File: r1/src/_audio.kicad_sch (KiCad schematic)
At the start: 24 parts, among them J10 PJ-320D, U7 PAM8908, U8 PCM5100A

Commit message: Assign MPN's and LCSC part numbers
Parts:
- D? (x2): LCSC (none) -> C261278
- J10: LCSC (none) -> C431535; MPN (none) -> PJ-320D
- U7: LCSC (none) -> C33233; MPN (none) -> PAM8908
- U8: value PCM5100A -> PCM5100APW; LCSC (none) -> C1540069; MPN (none) -> PCM5100APWR
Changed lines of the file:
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@@
       (effects (font (size 1.27 1.27)))
     )
-    (property "Value" "PCM5100A" (at 102.87 77.47 0)
+    (property "Value" "PCM5100APW" (at 102.87 77.47 0)
       (effects (font (size 1.27 1.27)))
     )
@@
     )
     (property "Datasheet" "http://www.ti.com/lit/ds/symlink/pcm5100.pdf" (at 92.71 73.66 0)
+      (effects (font (size 1.27 1.27)) hide)
+    )
+    (property "MPN" "PCM5100APWR" (at 93.98 92.71 0)
+      (effects (font (size 1.27 1.27)) hide)
+    )
+    (property "LCSC" "C1540069" (at 93.98 92.71 0)
       (effects (font (size 1.27 1.27)) hide)
     )
@@
       (effects (font (size 1.27 1.27)) hide)
     )
+    (property "MPN" "PAM8908" (at 180.34 99.06 0)
+      (effects (font (size 1.27 1.27)) hide)
+    )
+    (property "LCSC" "C33233" (at 180.34 99.06 0)
+      (effects (font (size 1.27 1.27)) hide)
+    )
     (pin "1")
     (pin "10")
@@
       (effects (font (size 1.27 1.27)) hide)
     )
+    (property "LCSC" "C261278" (at 222.25 93.98 0)
+      (effects (font (size 1.27 1.27)) hide)
+    )
     (pin "1")
     (pin "2")
@@
       (effects (font (size 1.27 1.27)) hide)
     )
+    (property "LCSC" "C261278" (at 214.63 93.98 0)
+      (effects (font (size 1.27 1.27)) hide)
+    )
     (pin "1")
     (pin "2")
@@
       (effects (font (size 1.27 1.27)) hide)
     )
+    (property "MPN" "PJ-320D" (at 236.22 90.17 0)
+      (effects (font (size 1.27 1.27)) hide)
+    )
+    (property "LCSC" "C431535" (at 236.22 90.17 0)
+      (effects (font (size 1.27 1.27)) hide)
+    )

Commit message: Assign manufacturers
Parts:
- J10: Manufacturer (none) -> HRO
- U7: Manufacturer (none) -> Diodes Incorporated
- U8: Manufacturer (none) -> Texas Instruments
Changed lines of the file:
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@@
+      (effects (font (size 1.27 1.27)) hide)
+    )
+    (property "Manufacturer" "Texas Instruments" (at 93.98 92.71 0)
       (effects (font (size 1.27 1.27)) hide)
     )
@@
       (effects (font (size 1.27 1.27)) hide)
     )
+    (property "Manufacturer" "Diodes Incorporated" (at 180.34 99.06 0)
+      (effects (font (size 1.27 1.27)) hide)
+    )
     (pin "1")
     (pin "10")
@@
       (effects (font (size 1.27 1.27)) hide)
     )
+    (property "Manufacturer" "HRO" (at 236.22 90.17 0)
+      (effects (font (size 1.27 1.27)) hide)
+    )

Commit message: Reannotate component refs
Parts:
- renumbered C38 to C12, C76 to C13, C41 to C14, C39 to C15, C40 to C16, C43 to C17, C42 to C18, C77 to C19, C44 to C20, C78 to C21, C79 to C22, C80 to C23, C81 to C24, C82 to C25, C83 to C26, C84 to C27, C85 to C28, C86 to C29, C87 to C30, J10 to J5, U8 to U4, U7 to U5

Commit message: Assign footprints from jeffmakes-footprints lib
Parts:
- D? (x2): footprint jeffmakes-footprints:SOD-523-numbered-pads -> jeffmakes_footprints:SOD-523-numbered-pads
- J5: footprint Connector_Audio:Jack_3.5mm_PJ320D_Horizontal_strengthening-vias -> jeffmakes_footprints:USB-A-short-body-in-cutout-type-strenghening-vias
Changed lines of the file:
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@@
       (effects (font (size 1.27 1.27)) (justify left))
     )
-    (property "Footprint" "jeffmakes-footprints:SOD-523-numbered-pads" (at 222.25 93.98 0)
+    (property "Footprint" "jeffmakes_footprints:SOD-523-numbered-pads" (at 222.25 93.98 0)
       (effects (font (size 1.27 1.27)) hide)
     )
@@
       (effects (font (size 1.27 1.27)) (justify left))
     )
-    (property "Footprint" "jeffmakes-footprints:SOD-523-numbered-pads" (at 214.63 93.98 0)
+    (property "Footprint" "jeffmakes_footprints:SOD-523-numbered-pads" (at 214.63 93.98 0)
       (effects (font (size 1.27 1.27)) hide)
     )
@@
       (effects (font (size 1.27 1.27)) (justify right))
     )
-    (property "Footprint" "Connector_Audio:Jack_3.5mm_PJ320D_Horizontal_strengthening-vias" (at 236.22 90.17 0)
+    (property "Footprint" "jeffmakes_footprints:USB-A-short-body-in-cutout-type-strenghening-vias" (at 236.22 90.17 0)
       (effects (font (size 1.27 1.27)) hide)
     )

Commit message: Assign footprints
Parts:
- J5: footprint jeffmakes_footprints:USB-A-short-body-in-cutout-type-strenghening-vias -> jeffmakes_footprints:Jack_3.5mm_PJ320D_Horizontal_strengthening-vias
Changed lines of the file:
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@@
       (effects (font (size 1.27 1.27)) (justify right))
     )
-    (property "Footprint" "jeffmakes_footprints:USB-A-short-body-in-cutout-type-strenghening-vias" (at 236.22 90.17 0)
+    (property "Footprint" "jeffmakes_footprints:Jack_3.5mm_PJ320D_Horizontal_strengthening-vias" (at 236.22 90.17 0)
       (effects (font (size 1.27 1.27)) hide)
     )

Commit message: ERC pass. Schematic complete.
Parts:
- D? (x2): footprint jeffmakes_footprints:SOD-523-numbered-pads -> jeffmakes-footprints:SOD-523-numbered-pads
- J5: footprint jeffmakes_footprints:Jack_3.5mm_PJ320D_Horizontal_strengthening-vias -> jeffmakes-footprints:Jack_3.5mm_PJ320D_Horizontal_strengthening-vias
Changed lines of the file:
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@@
       (effects (font (size 1.27 1.27)) (justify left))
     )
-    (property "Footprint" "jeffmakes_footprints:SOD-523-numbered-pads" (at 222.25 93.98 0)
+    (property "Footprint" "jeffmakes-footprints:SOD-523-numbered-pads" (at 222.25 93.98 0)
       (effects (font (size 1.27 1.27)) hide)
     )
@@
       (effects (font (size 1.27 1.27)) (justify left))
     )
-    (property "Footprint" "jeffmakes_footprints:SOD-523-numbered-pads" (at 214.63 93.98 0)
+    (property "Footprint" "jeffmakes-footprints:SOD-523-numbered-pads" (at 214.63 93.98 0)
       (effects (font (size 1.27 1.27)) hide)
     )
@@
       (effects (font (size 1.27 1.27)) (justify right))
     )
-    (property "Footprint" "jeffmakes_footprints:Jack_3.5mm_PJ320D_Horizontal_strengthening-vias" (at 236.22 90.17 0)
+    (property "Footprint" "jeffmakes-footprints:Jack_3.5mm_PJ320D_Horizontal_strengthening-vias" (at 236.22 90.17 0)
       (effects (font (size 1.27 1.27)) hide)
     )

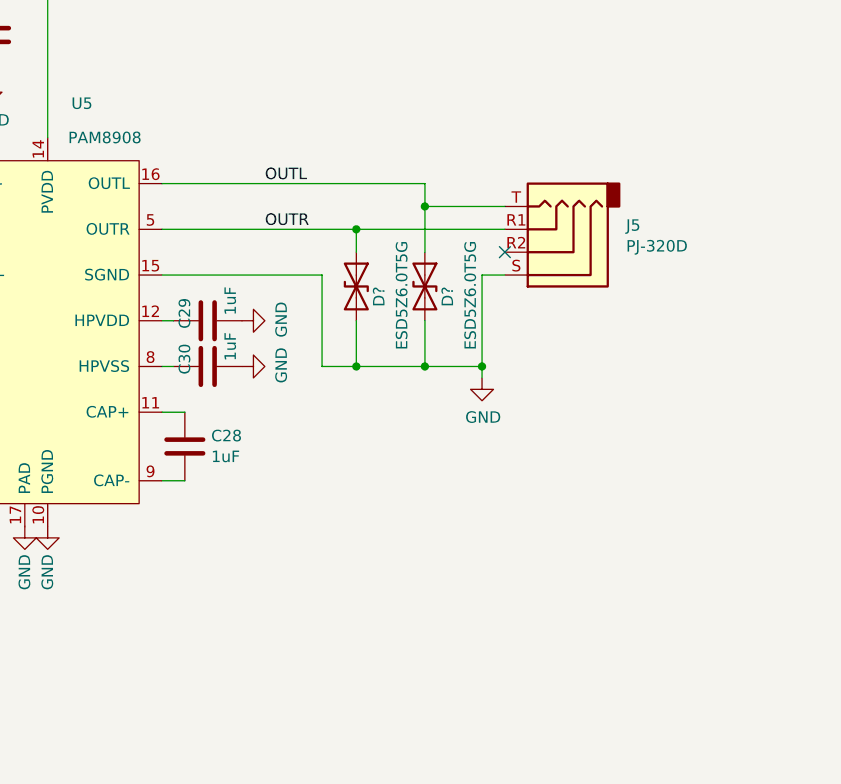
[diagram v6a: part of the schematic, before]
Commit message: Speaker connector and mute switch
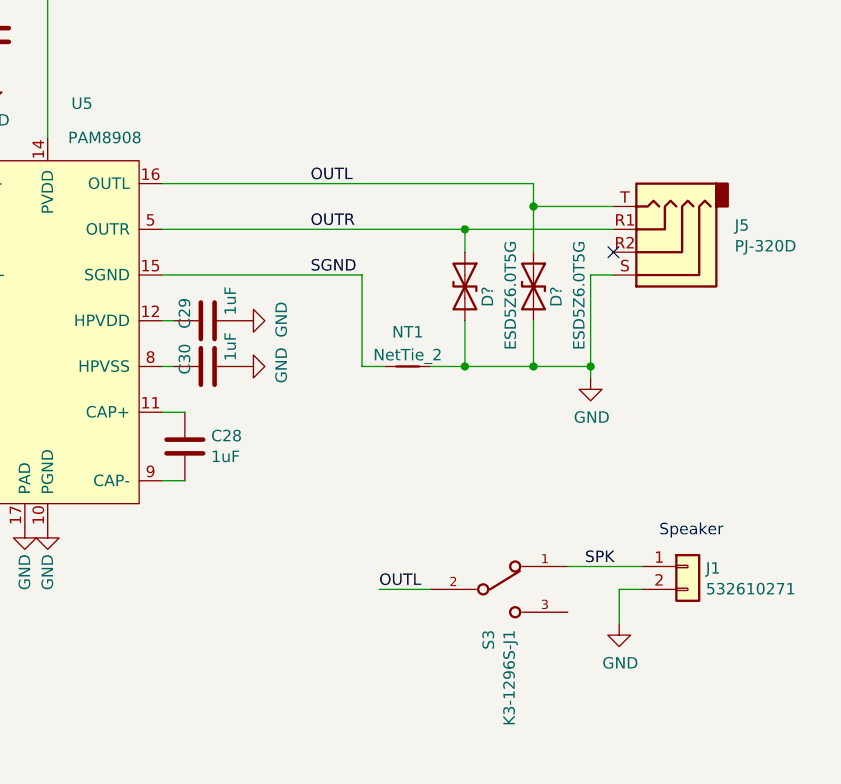
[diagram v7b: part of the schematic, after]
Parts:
- added J1: 532610271, Connector_Molex:Molex_PicoBlade_53261-0271_1x02-1MP_P1.25mm_Horizontal, symbol Connector_Generic:Conn_01x02
- added NT1: NetTie_2, NetTie:NetTie-2_SMD_Pad0.5mm, symbol Device:NetTie_2
- added S3: K3-1296S-J1, Button_Switch_SMD:SW_SPDT_PCM12, symbol j_Switch:JS102011SAQN
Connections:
- net GND: now also J1.2 (Pin_2), NT1.2; no longer U5.15 (SGND)
- net OUTL: now also S3.2
- new net SGND: NT1.1, U5.15 (SGND)
- new net SPK: J1.1 (Pin_1), S3.1
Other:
- note added: "Speaker"
- moved on the sheet: D?, J5
